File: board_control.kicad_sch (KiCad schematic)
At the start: 14 parts

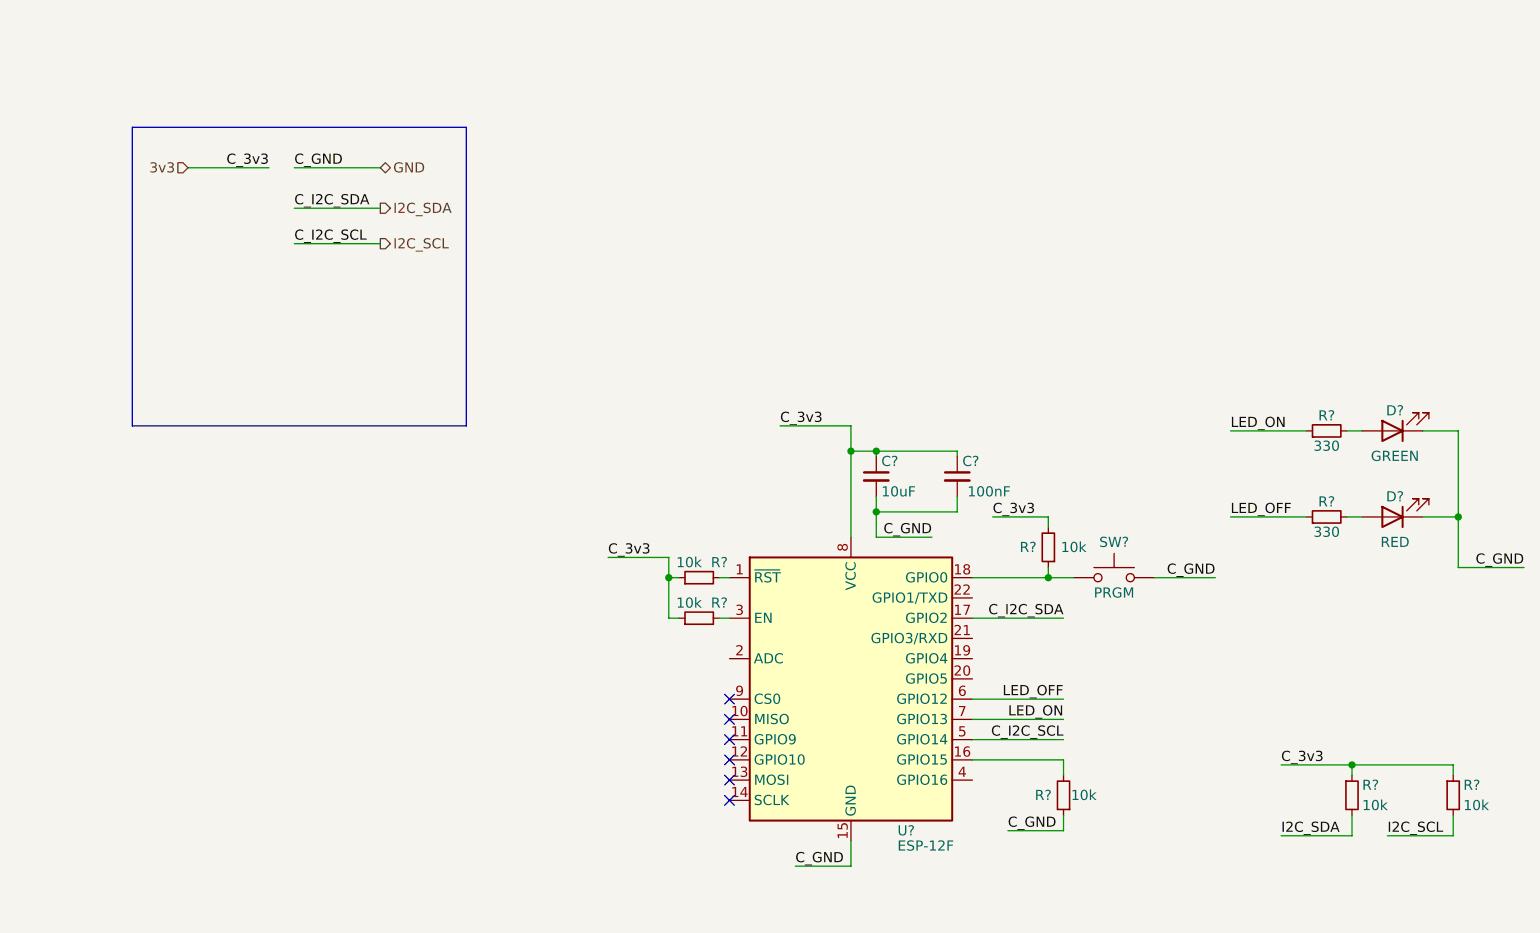
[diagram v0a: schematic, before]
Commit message: Fixed file name, started board layout
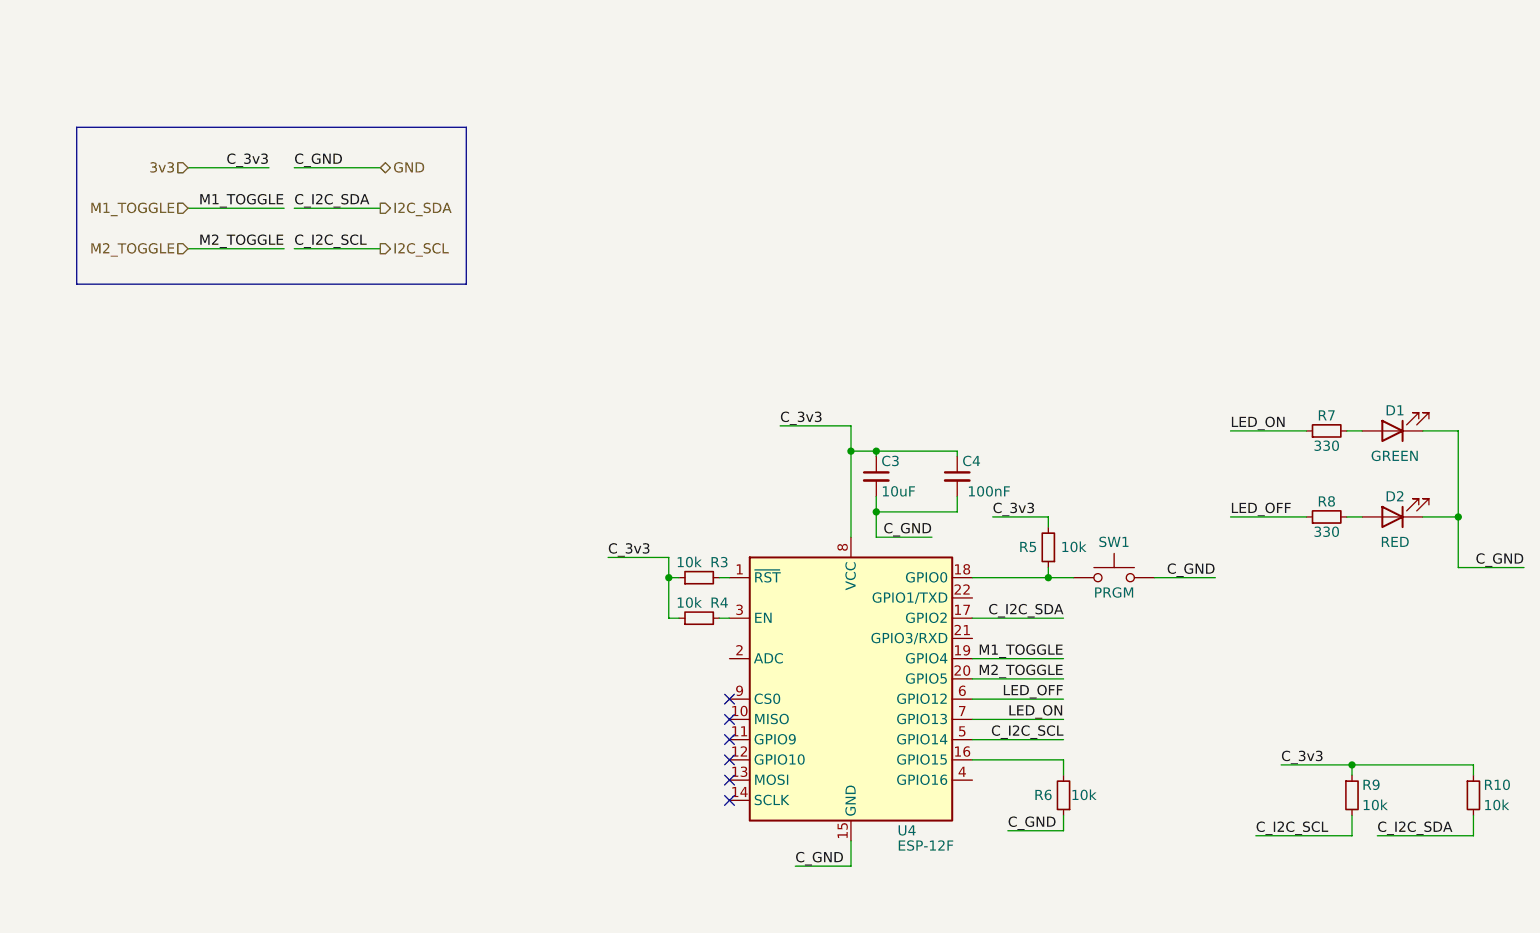
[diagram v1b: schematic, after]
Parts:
- removed R?: 10k, symbol Device:R_Small
- added R9: 10k, Resistor_SMD:R_0402_1005Metric, symbol Device:R_Small
- C3, C4: renamed from C?; footprint (none) -> Capacitor_SMD:C_0402_1005Metric
- R10, R3, R4, R5, R6, R7, R8: renamed from R?; footprint (none) -> Resistor_SMD:R_0402_1005Metric
- gave numbers to parts that had none: 4
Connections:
- net 3v3: now also R9.1
- net I2C_SCL: now also R9.2; no longer R10.2
- net I2C_SDA: now also R10.2
- net M1_TOGGLE: now reaches U4.19 (GPIO4)
- net M2_TOGGLE: now reaches U4.20 (GPIO5)
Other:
- moved on the sheet: R10

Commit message: Updated board connections. Added supplier info for all parts
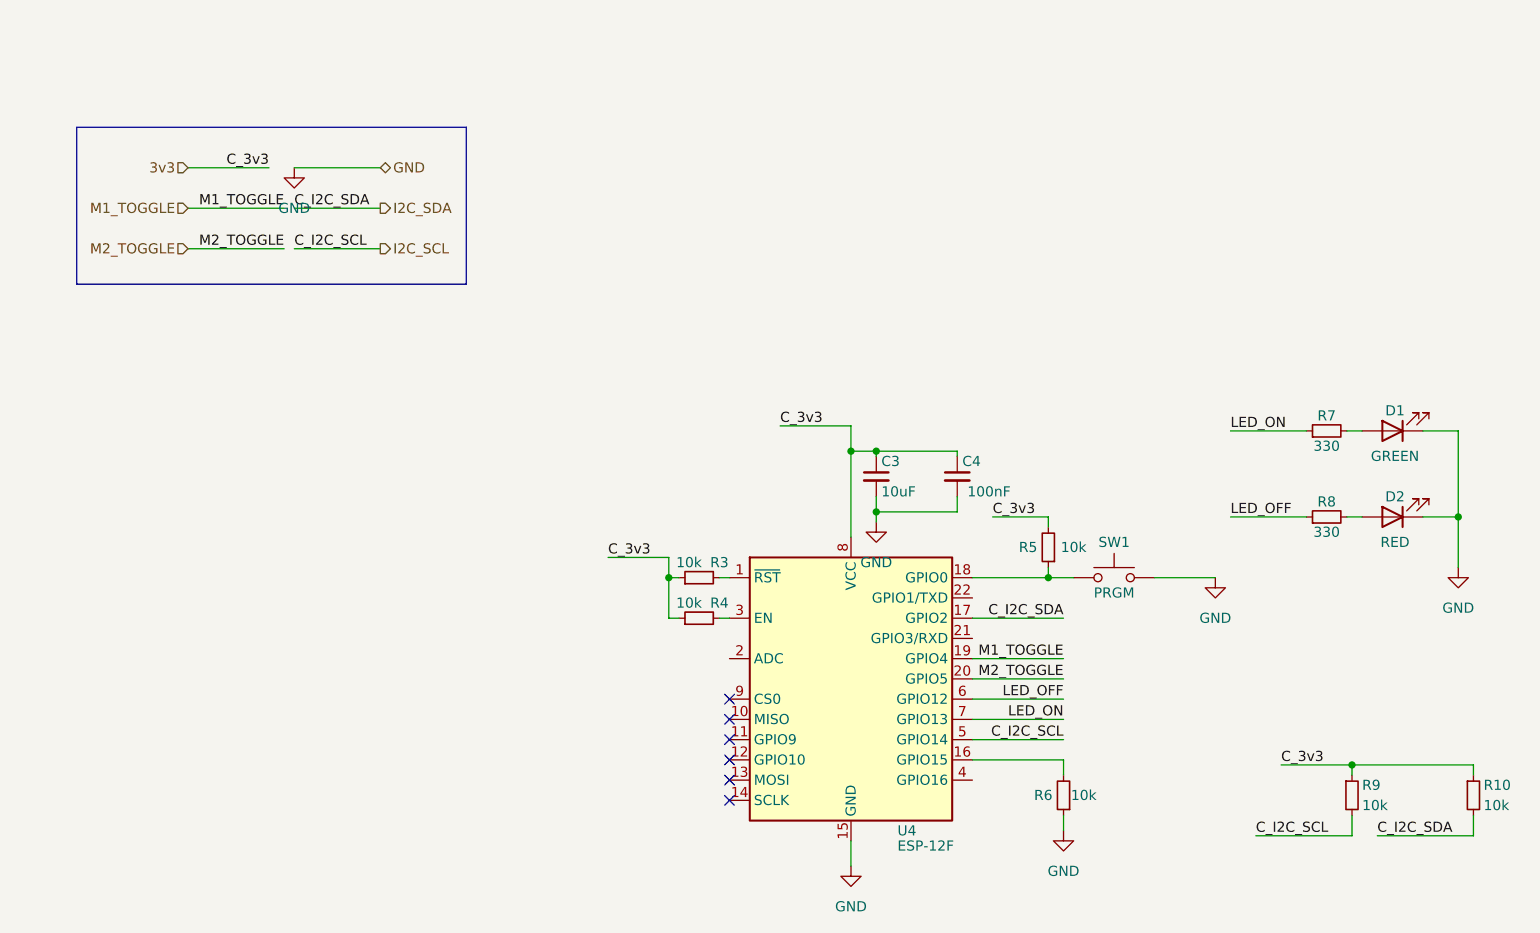
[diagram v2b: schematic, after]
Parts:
- C3: footprint Capacitor_SMD:C_0402_1005Metric -> Capacitor_SMD:C_0603_1608Metric; LCSC Part Number (none) -> C100042; Manufacturer (none) -> YAGEO; Manufacturer Part Number (none) -> CC0603KRX7R9BB103
- C4: footprint Capacitor_SMD:C_0402_1005Metric -> Capacitor_SMD:C_0603_1608Metric; LCSC Part Number (none) -> C30926; Manufacturer (none) -> FH (Guangdong Fenghua Advanced Tech); Manufacturer Part Number (none) -> 0603B104K500NT
- D1: footprint (none) -> LED_SMD:LED_0805_2012Metric; LCSC Part Number (none) -> C434432; Manufacturer (none) -> Yongyu Photoelectric; Manufacturer Part Number (none) -> SZYY0805G
- D2: footprint (none) -> LED_SMD:LED_0805_2012Metric; LCSC Part Number (none) -> C84256; Manufacturer (none) -> Foshan NationStar Optoelectronics; Manufacturer Part Number (none) -> NCD0805R1
- R10, R3, R4, R5, R6, R9: footprint Resistor_SMD:R_0402_1005Metric -> Resistor_SMD:R_0201_0603Metric; LCSC Part Number (none) -> C99198; Manufacturer (none) -> YAGEO; Manufacturer Part Number (none) -> RC0603JR-0710KL
- R7, R8: footprint Resistor_SMD:R_0402_1005Metric -> Resistor_SMD:R_0201_0603Metric; LCSC Part Number (none) -> C25229; Manufacturer (none) -> UNI-ROYAL(Uniroyal Elec); Manufacturer Part Number (none) -> 0603WAJ0301T5E
- SW1: footprint (none) -> Library:TS-1187A-B-A-B; LCSC Part Number (none) -> C318884; Manufacturer (none) -> XKB Connectivity; Manufacturer Part Number (none) -> TS-1187A-B-A-B
- U4: LCSC Part Number (none) -> C82891; Manufacturer (none) -> Ai-Thinker; Manufacturer Part Number (none) -> ESP-12F(ESP8266MOD)

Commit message: Did work on schematic
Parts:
- D2: value RED -> GREEN; LCSC Part Number C84256 -> C434432; Manufacturer Foshan NationStar Optoelectronics -> Yongyu Photoelectric; Manufacturer Part Number NCD0805R1 -> SZYY0805G
- R10, R3, R4, R5, R6, R7, R8, R9: footprint Resistor_SMD:R_0201_0603Metric -> Resistor_SMD:R_0603_1608Metric
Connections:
- net LED_OFF renamed LED_2
- net LED_ON renamed LED_1
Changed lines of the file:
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@@
     (effects (font (size 1.27 1.27)) (justify left bottom))
   )
-  (label "LED_ON" (at 144.78 100.33 180)
+  (label "LED_1" (at 144.78 100.33 180)
     (effects (font (size 1.27 1.27)) (justify right bottom))
   )
@@
     (effects (font (size 1.27 1.27)) (justify right bottom))
   )
-  (label "LED_OFF" (at 144.78 97.79 180)
+  (label "LED_2" (at 144.78 97.79 180)
     (effects (font (size 1.27 1.27)) (justify right bottom))
   )
@@
     (effects (font (size 1.27 1.27)) (justify left bottom))
   )
-  (label "LED_ON" (at 165.735 64.135 0)
-    (effects (font (size 1.27 1.27)) (justify left bottom))
-  )
-  (label "LED_OFF" (at 165.735 74.93 0)
+  (label "LED_1" (at 165.735 64.135 0)
+    (effects (font (size 1.27 1.27)) (justify left bottom))
+  )
+  (label "LED_2" (at 165.735 74.93 0)
     (effects (font (size 1.27 1.27)) (justify left bottom))
   )
@@
       (effects (font (size 1.27 1.27)) (justify left))
     )
-    (property "Footprint" "Resistor_SMD:R_0201_0603Metric" (id 2) (at 180.975 109.855 0)
+    (property "Footprint" "Resistor_SMD:R_0603_1608Metric" (id 2) (at 180.975 109.855 0)
       (effects (font (size 1.27 1.27)) hide)
     )
@@
     (property "Reference" "R4" (id 0) (at 101.6 85.725 90))
     (property "Value" "10k" (id 1) (at 97.79 85.725 90))
-    (property "Footprint" "Resistor_SMD:R_0201_0603Metric" (id 2) (at 99.06 87.63 0)
+    (property "Footprint" "Resistor_SMD:R_0603_1608Metric" (id 2) (at 99.06 87.63 0)
       (effects (font (size 1.27 1.27)) hide)
     )
@@
     (property "Reference" "R8" (id 0) (at 177.8 73.025 90))
     (property "Value" "330" (id 1) (at 177.8 76.835 90))
-    (property "Footprint" "Resistor_SMD:R_0201_0603Metric" (id 2) (at 177.8 74.93 0)
+    (property "Footprint" "Resistor_SMD:R_0603_1608Metric" (id 2) (at 177.8 74.93 0)
       (effects (font (size 1.27 1.27)) hide)
     )
@@
     )
     (property "Manufacturer Part Number" "0603WAJ0301T5E" (id 6) (at 177.8 74.93 0)
-      (effects (font (size 1.27 1.27)) hide)
-    )
-    (pin "1")
-    (pin "2")
-  )
-  (symbol (lib_id "Device:LED") (at 186.055 74.93 180) (unit 1)
-    (in_bom yes) (on_board yes)
-    (property "Reference" "D2" (id 0) (at 186.3725 72.39 0))
-    (property "Value" "RED" (id 1) (at 186.3725 78.105 0))
-    (property "Footprint" "LED_SMD:LED_0805_2012Metric" (id 2) (at 186.055 74.93 0)
-      (effects (font (size 1.27 1.27)) hide)
-    )
-    (property "Datasheet" "~" (id 3) (at 186.055 74.93 0)
-      (effects (font (size 1.27 1.27)) hide)
-    )
-    (property "LCSC Part Number" "C84256" (id 4) (at 186.055 74.93 0)
-      (effects (font (size 1.27 1.27)) hide)
-    )
-    (property "Manufacturer" "Foshan NationStar Optoelectronics" (id 5) (at 186.055 74.93 0)
-      (effects (font (size 1.27 1.27)) hide)
-    )
-    (property "Manufacturer Part Number" "NCD0805R1" (id 6) (at 186.055 74.93 0)
       (effects (font (size 1.27 1.27)) hide)
     )
@@
     (property "Reference" "R7" (id 0) (at 177.8 62.23 90))
     (property "Value" "330" (id 1) (at 177.8 66.04 90))
-    (property "Footprint" "Resistor_SMD:R_0201_0603Metric" (id 2) (at 177.8 64.135 0)
+    (property "Footprint" "Resistor_SMD:R_0603_1608Metric" (id 2) (at 177.8 64.135 0)
       (effects (font (size 1.27 1.27)) hide)
     )
@@
     (property "Reference" "R3" (id 0) (at 101.6 80.645 90))
     (property "Value" "10k" (id 1) (at 97.79 80.645 90))
-    (property "Footprint" "Resistor_SMD:R_0201_0603Metric" (id 2) (at 99.06 82.55 0)
+    (property "Footprint" "Resistor_SMD:R_0603_1608Metric" (id 2) (at 99.06 82.55 0)
       (effects (font (size 1.27 1.27)) hide)
     )
@@
     (pin "2")
   )
+  (symbol (lib_id "Device:LED") (at 186.055 74.93 180) (unit 1)
+    (in_bom yes) (on_board yes)
+    (property "Reference" "D2" (id 0) (at 186.3725 72.39 0))
+    (property "Value" "GREEN" (id 1) (at 186.3725 78.105 0))
+    (property "Footprint" "LED_SMD:LED_0805_2012Metric" (id 2) (at 186.055 74.93 0)
+      (effects (font (size 1.27 1.27)) hide)
+    )
+    (property "Datasheet" "~" (id 3) (at 186.055 74.93 0)
+      (effects (font (size 1.27 1.27)) hide)
+    )
+    (property "LCSC Part Number" "C434432" (id 4) (at 186.055 74.93 0)
+      (effects (font (size 1.27 1.27)) hide)
+    )
+    (property "Manufacturer" "Yongyu Photoelectric" (id 5) (at 186.055 74.93 0)
+      (effects (font (size 1.27 1.27)) hide)
+    )
+    (property "Manufacturer Part Number" "SZYY0805G" (id 6) (at 186.055 74.93 0)
+      (effects (font (size 1.27 1.27)) hide)
+    )
+    (pin "1")
+    (pin "2")
+  )
   (symbol (lib_id "power:GND") (at 194.31 81.28 0) (unit 1)
     (in_bom yes) (on_board yes) (fields_autoplaced)
@@
       (effects (font (size 1.27 1.27)) (justify left))
     )
-    (property "Footprint" "Resistor_SMD:R_0201_0603Metric" (id 2) (at 196.215 109.855 0)
+    (property "Footprint" "Resistor_SMD:R_0603_1608Metric" (id 2) (at 196.215 109.855 0)
       (effects (font (size 1.27 1.27)) hide)
     )
@@
     (property "Reference" "R6" (id 0) (at 142.24 109.855 0))
     (property "Value" "10k" (id 1) (at 147.32 109.855 0))
-    (property "Footprint" "Resistor_SMD:R_0201_0603Metric" (id 2) (at 144.78 109.855 0)
+    (property "Footprint" "Resistor_SMD:R_0603_1608Metric" (id 2) (at 144.78 109.855 0)
       (effects (font (size 1.27 1.27)) hide)
     )
@@
     (property "Reference" "R5" (id 0) (at 140.335 78.74 0))
     (property "Value" "10k" (id 1) (at 146.05 78.74 0))
-    (property "Footprint" "Resistor_SMD:R_0201_0603Metric" (id 2) (at 142.875 78.74 0)
-      (effects (font (size 1.27 1.27)) hide)
-    )
+    (property "Footprint" "Resistor_SMD:R_0603_1608Metric" (id 2) (at 142.875 78.74 0)
+      (effects (font (size 1.27 1.27)) hide)
+    )

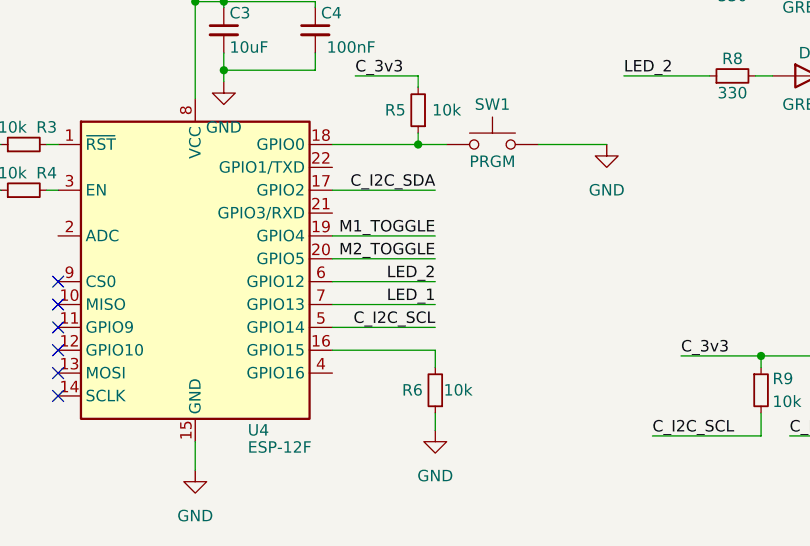
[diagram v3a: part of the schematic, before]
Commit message: Finished initial layout of PCB
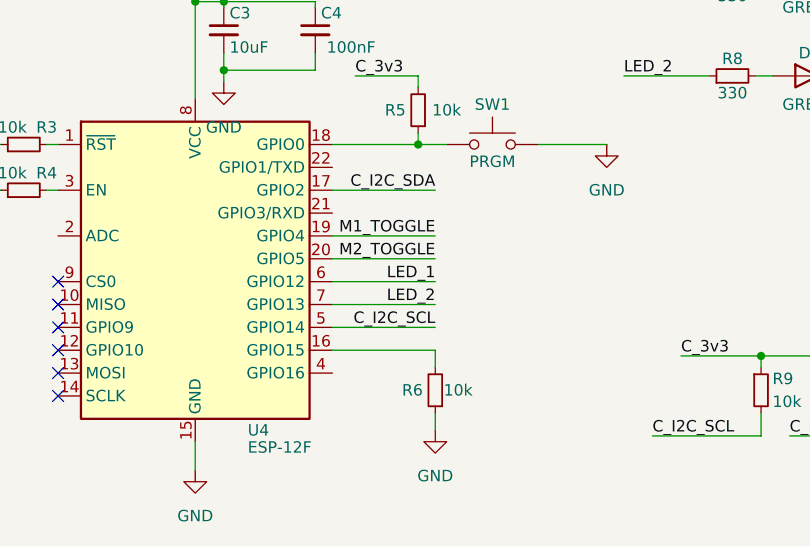
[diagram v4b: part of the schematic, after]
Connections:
- net LED_1: now also U4.6 (GPIO12); no longer U4.7 (GPIO13)
- net LED_2: now also U4.7 (GPIO13); no longer U4.6 (GPIO12)
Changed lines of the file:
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@@
     (effects (font (size 1.27 1.27)) (justify left bottom))
   )
-  (label "LED_1" (at 144.78 100.33 180)
+  (label "LED_1" (at 144.78 97.79 180)
     (effects (font (size 1.27 1.27)) (justify right bottom))
   )
@@
   )
   (label "M2_TOGGLE" (at 144.78 95.25 180)
+    (effects (font (size 1.27 1.27)) (justify right bottom))
+  )
+  (label "LED_2" (at 144.78 100.33 180)
     (effects (font (size 1.27 1.27)) (justify right bottom))
   )
@@
     (effects (font (size 1.27 1.27)) (justify right bottom))
   )
-  (label "LED_2" (at 144.78 97.79 180)
-    (effects (font (size 1.27 1.27)) (justify right bottom))
-  )
